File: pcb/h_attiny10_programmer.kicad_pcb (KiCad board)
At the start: 2 copper layers, 100 x 80 mm, 60 parts, among them J1 PWR, J2 Conn_01x03, J3 Conn_01x03, J4 Conn_01x03, J5 Conn_01x03, J6 Conn_01x03, J7 Conn_01x03, J8 AVR-TPI-6, Q1 2N3906, SW1 SW_Push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

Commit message: PNP incorrect orientaiton, mirrored along x axis in schematic to fix
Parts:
- moved Q1 5.10 mm to (181.6, 86.0), turned to 180 degrees
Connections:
- Q1 pad 1: PROG_12V -> +12V
- Q1 pad 3: +12V -> PROG_12V
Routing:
- net PROG_12V: track 30.6 -> 37.2 mm
- net +12V: track 12.3 -> 16.2 mm
- net Net-(Q1-Pad2): track 10.4 -> 13.4 mm

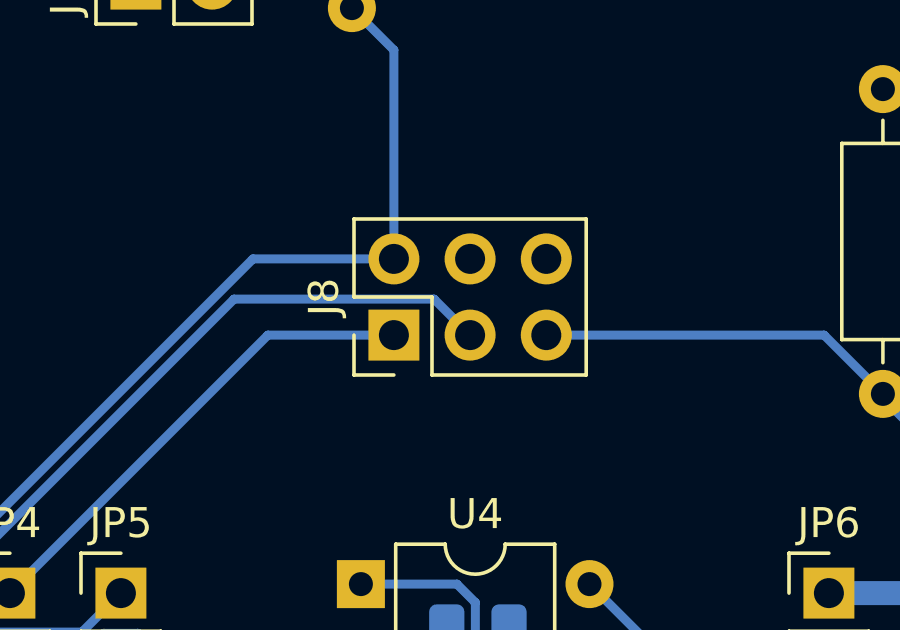
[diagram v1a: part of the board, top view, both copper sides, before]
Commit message: connect TPIDATA to MISO and MOSI
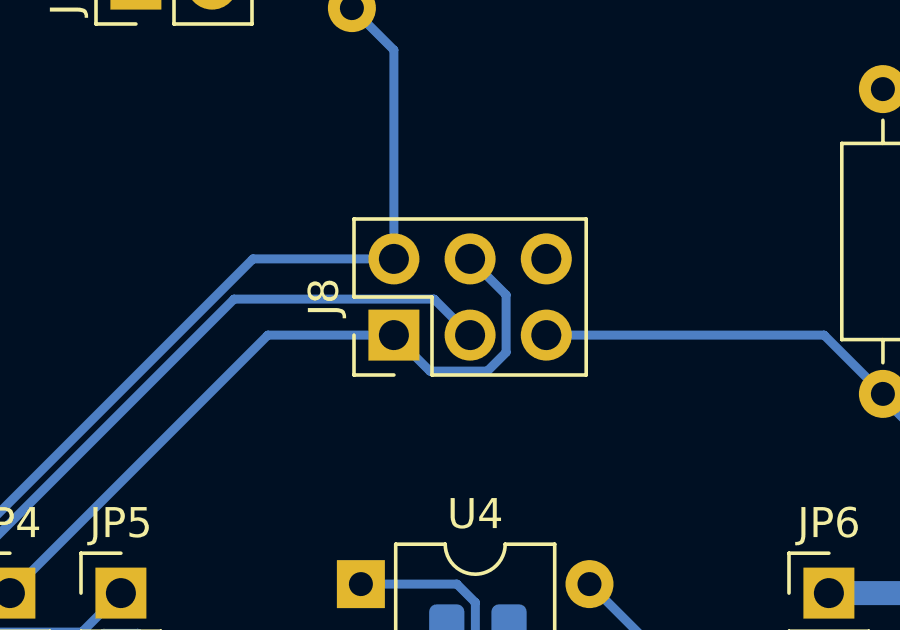
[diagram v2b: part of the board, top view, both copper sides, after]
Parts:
- J8: value AVR-TPI-6 -> USBasp-ISP
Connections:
- J8 pad 4: Net-(J8-Pad4) -> DATA
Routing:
- net DATA: track 16.4 -> 24.5 mm
